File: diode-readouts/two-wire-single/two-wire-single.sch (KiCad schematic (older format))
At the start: 9 parts, among them J1 Conn_01x04, J2 JST_SH_Conn_01x04_i2c_horizon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, J3 Conn_01x01_Female

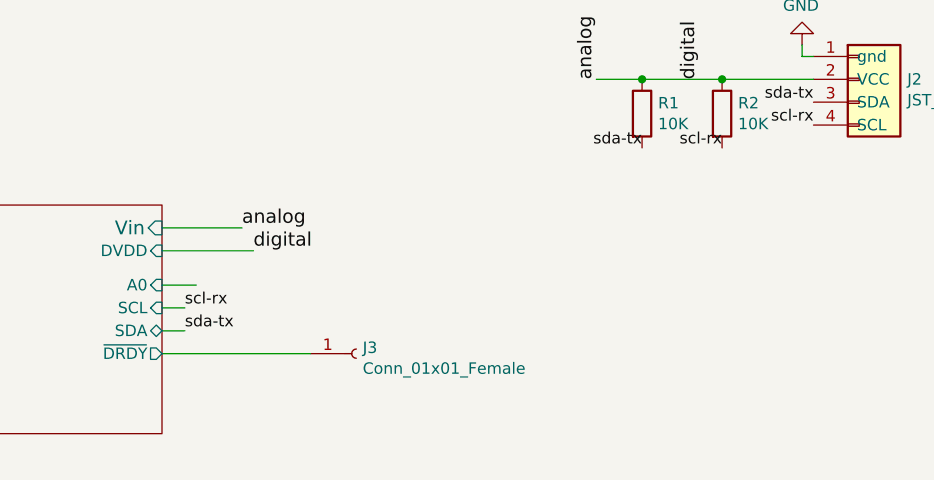
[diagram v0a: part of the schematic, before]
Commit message: Add 47ohms for compatibility with ADS122U04.
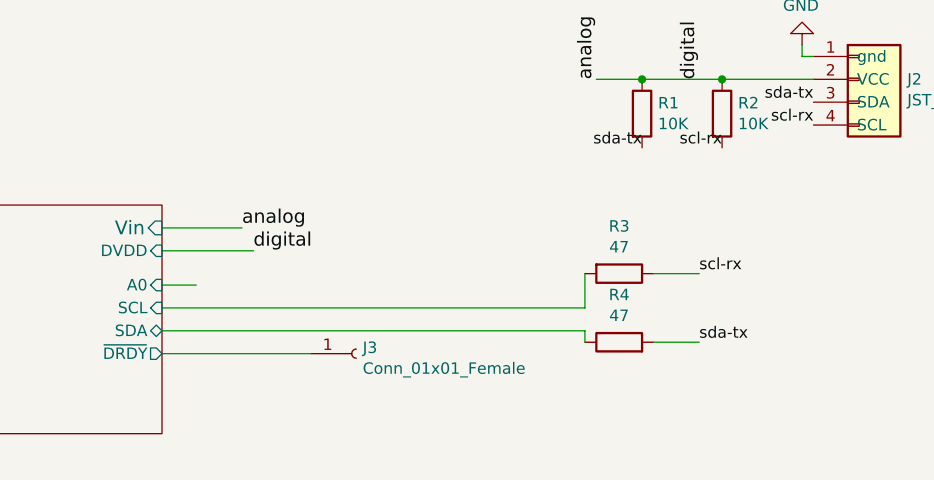
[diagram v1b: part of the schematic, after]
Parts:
- added R3, R4: 47, Resistor_SMD:R_0402_1005Metric, symbol 0JLC:R
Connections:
- wire segments 28 -> 32
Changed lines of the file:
@@
 Text Label 7300 3450 2    50   ~ 0
 sda-tx
-Text Label 4550 4350 0    50   ~ 0
+Text Label 6800 4200 0    50   ~ 0
 scl-rx
-Text Label 4550 4450 0    50   ~ 0
+Text Label 6800 4500 0    50   ~ 0
 sda-tx
-Wire Wire Line
-	4450 4350 4550 4350
-Wire Wire Line
-	4550 4450 4450 4450
 Text Label 4850 4100 0    60   ~ 0
 digital
@@
 Wire Wire Line
 	4450 4550 5100 4550
+$Comp
+L 0JLC:R R3
+U 1 1 6249D4AC
+P 6450 4200
+F 0 "R3" V 6243 4200 50  0000 C CNN
+F 1 "47" V 6334 4200 50  0000 C CNN
+F 2 "Resistor_SMD:R_0402_1005Metric" V 6380 4200 50  0001 C CNN
+F 3 "~" H 6450 4200 50  0001 C CNN
+F 4 "C25168" V 6450 4200 50  0001 C CNN "LCSC"
+F 5 "0402WGJ0470TCE" V 6450 4200 50  0001 C CNN "MPN"
+	1    6450 4200
+	0    1    1    0
+$EndComp
+$Comp
+L 0JLC:R R4
+U 1 1 6249E18D
+P 6450 4500
+F 0 "R4" V 6657 4500 50  0000 C CNN
+F 1 "47" V 6566 4500 50  0000 C CNN
+F 2 "Resistor_SMD:R_0402_1005Metric" V 6380 4500 50  0001 C CNN
+F 3 "~" H 6450 4500 50  0001 C CNN
+F 4 "C25168" V 6450 4500 50  0001 C CNN "LCSC"
+F 5 "0402WGJ0470TCE" V 6450 4500 50  0001 C CNN "MPN"
+	1    6450 4500
+	0    -1   -1   0
+$EndComp
+Wire Wire Line
+	6300 4350 6300 4200
+Wire Wire Line
+	4450 4350 6300 4350
+Wire Wire Line
+	6300 4450 6300 4500
+Wire Wire Line
+	4450 4450 6300 4450
+Wire Wire Line
+	6600 4200 6800 4200
+Wire Wire Line
+	6800 4500 6600 4500
 $EndSCHEMATC
